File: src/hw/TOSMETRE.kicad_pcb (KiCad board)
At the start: 2 copper layers, 4.5 x 3.5 mm, 61 parts, among them J1 Barrel_Jack_Switch, J2 Conn_01x02_Male, J3 Conn_01x08_Male, J4 Conn_Coaxial, J5 Conn_01x05_Male, J6 Conn_01x02_Male, J7 Conn_Coaxial, SW1 SW_DIP_x01, U1 TPS70950DBVT, U2 18F1320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

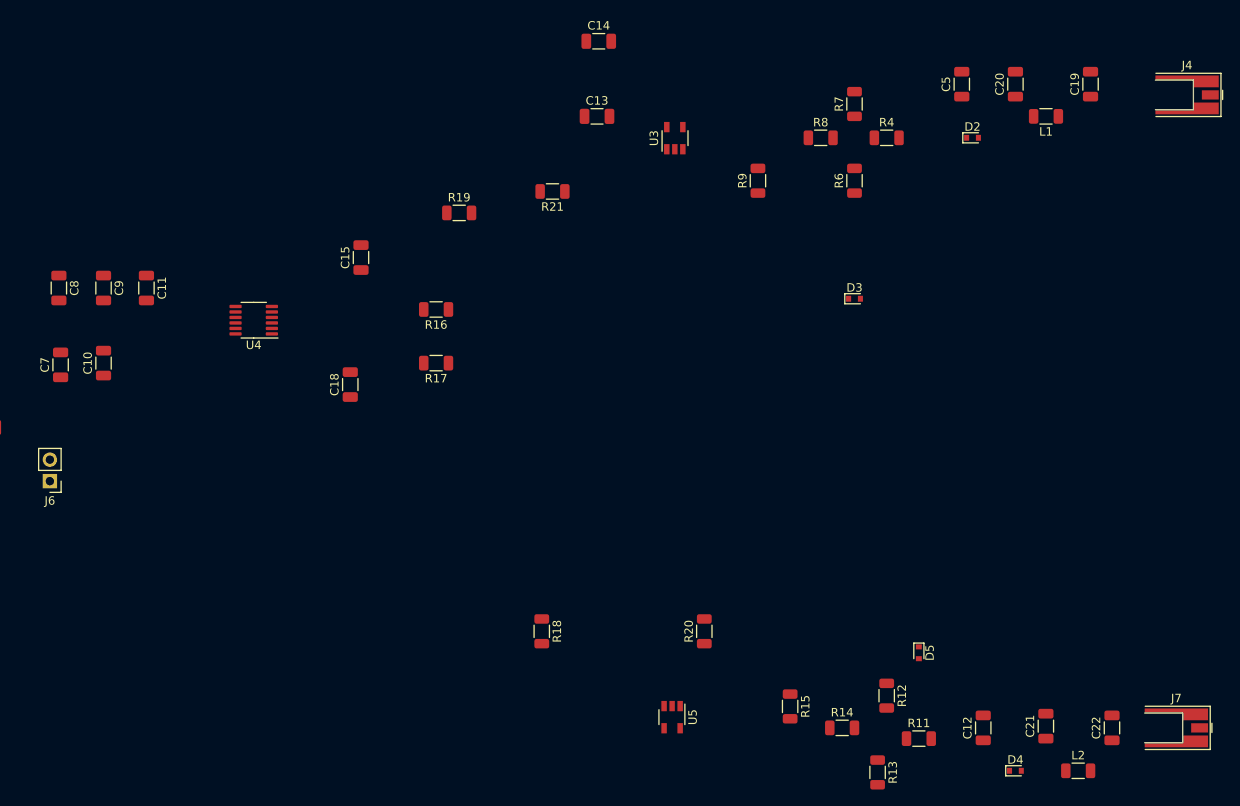
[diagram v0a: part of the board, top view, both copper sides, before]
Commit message: #305
debut routage pour degrossir et se rendre compte
a optimiser
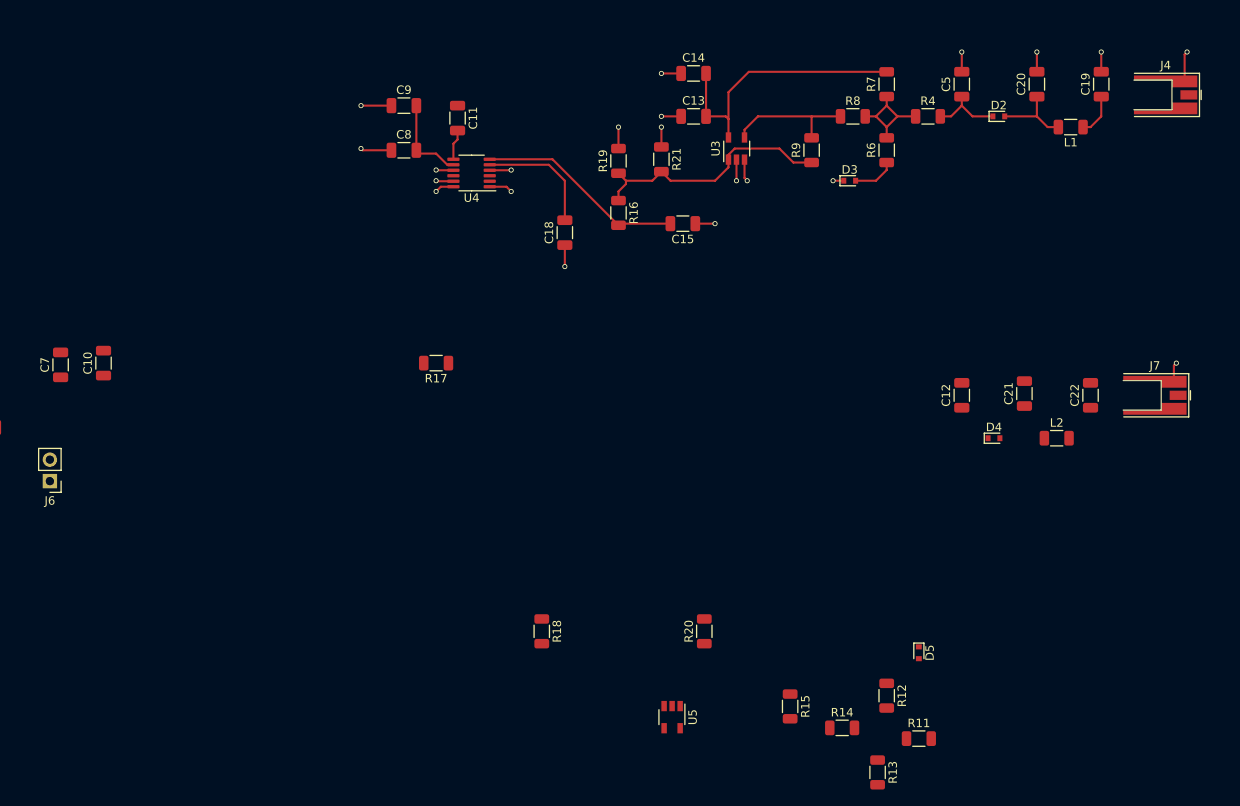
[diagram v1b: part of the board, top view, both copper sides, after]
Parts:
- moved C8 44.0 mm to (166.4, 45.9), turned to 0 degrees
- moved C11 42.0 mm to (172.7, 42.1)
- moved C9 41.6 mm to (166.4, 40.6), turned to 0 degrees
- moved C21 39.5 mm to (239.8, 74.7)
- moved C12 39.5 mm to (232.4, 74.9)
- moved C22 39.5 mm to (247.7, 74.9)
- moved D4 39.5 mm to (236.2, 80.0)
- moved J7 39.5 mm to (255.3, 74.9)
- moved L2 39.5 mm to (243.6, 80.0)
- moved C15 38.3 mm to (199.4, 54.6), turned to 180 degrees
- moved U4 31.1 mm to (174.4, 48.6)
- moved C18 31.1 mm to (185.4, 55.7)
- moved R16 24.4 mm to (191.8, 53.3), turned to 270 degrees
- moved R19 19.8 mm to (191.8, 47.2), turned to 90 degrees
- moved D3 14.0 mm to (219.1, 49.5)
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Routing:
- net GNDREF: track 0.00 -> 52.8 mm, vias 0 -> 21
- net Net-(C13-Pad2): track 0.00 -> 33.0 mm
- net Net-(R16-Pad1): track 0.00 -> 30.0 mm
- net Net-(C15-Pad2): track 0.00 -> 24.7 mm
- net Net-(R8-Pad1): track 0.00 -> 15.5 mm
- net Net-(C18-Pad2): track 0.00 -> 14.3 mm
- net Net-(R4-Pad1): track 0.00 -> 13.0 mm
- net Net-(C8-Pad2): track 0.00 -> 10.4 mm
- net Net-(C20-Pad1): track 0.00 -> 9.21 mm
- net Net-(C5-Pad1): track 0.00 -> 8.34 mm
- net Net-(D3-Pad2): track 0.00 -> 5.09 mm
- net Net-(C19-Pad1): track 0.00 -> 5.02 mm
- net Net-(C11-Pad2): track 0.00 -> 3.60 mm

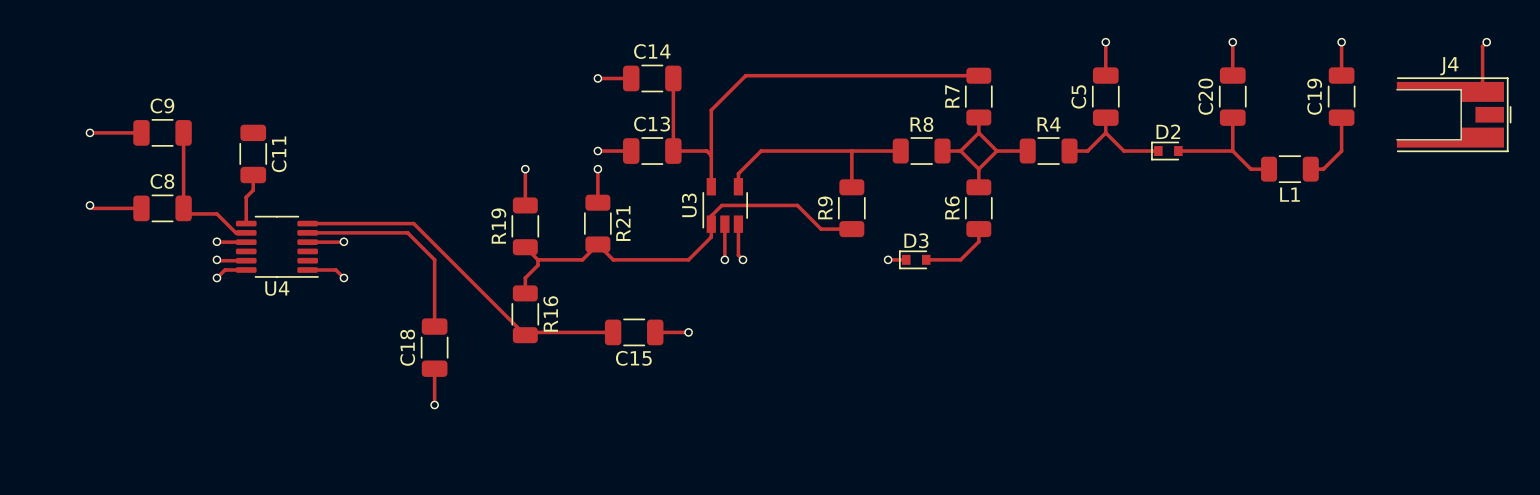
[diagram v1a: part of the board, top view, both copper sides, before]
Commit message: #305
pour validation
Pise 1mm
via  diametre 1,4 et percage de 0,6
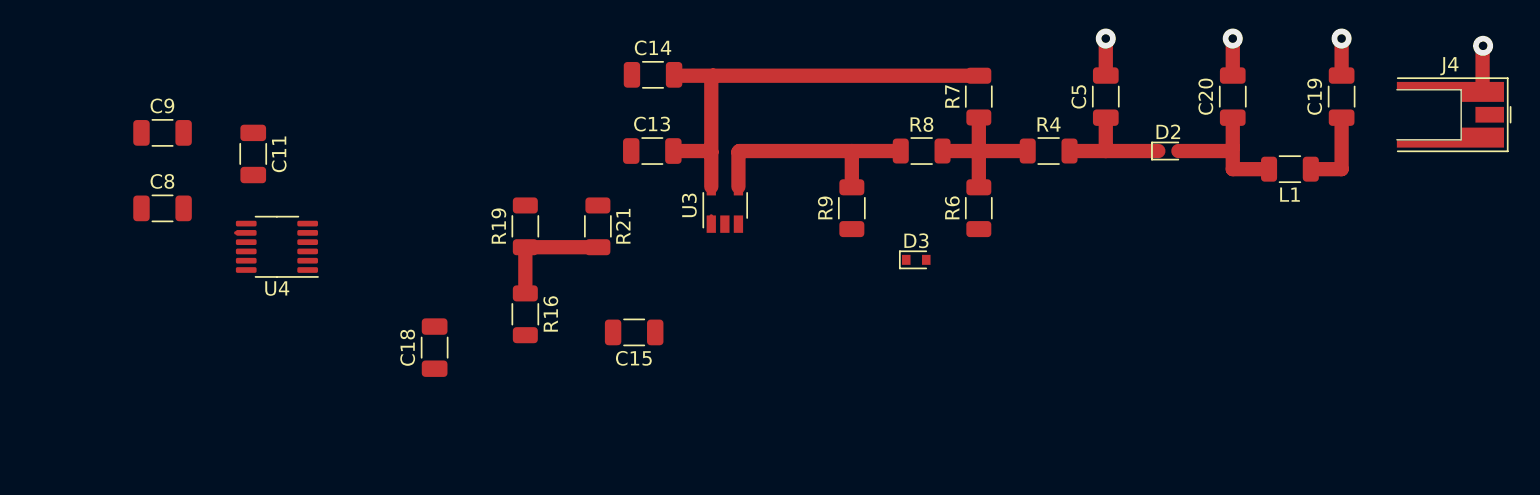
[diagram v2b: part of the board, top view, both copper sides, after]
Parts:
- moved C14 0.26 mm to (200.7, 36.6)
- moved R21 0.19 mm to (196.8, 47.2)
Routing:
- net GNDREF: track 52.8 -> 13.3 mm, vias 21 -> 5
- net Net-(C15-Pad2): track 24.7 -> 0.27 mm
- net Net-(R16-Pad1): track 30.0 -> 8.88 mm
- net Net-(C18-Pad2): track 14.3 -> 0.00 mm
- net Net-(C8-Pad2): track 10.4 -> 1.28 mm
- net Net-(D3-Pad2): track 5.09 -> 0.00 mm
- net Net-(C11-Pad2): track 3.60 -> 0.00 mm
- net Net-(R4-Pad1): track 13.0 -> 11.1 mm
- net Net-(C13-Pad2): track 33.0 -> 31.9 mm
- net Net-(R8-Pad1): track 15.5 -> 16.4 mm
- net Net-(C20-Pad1): track 9.21 -> 10.1 mm
- net Net-(C19-Pad1): track 5.02 -> 5.76 mm

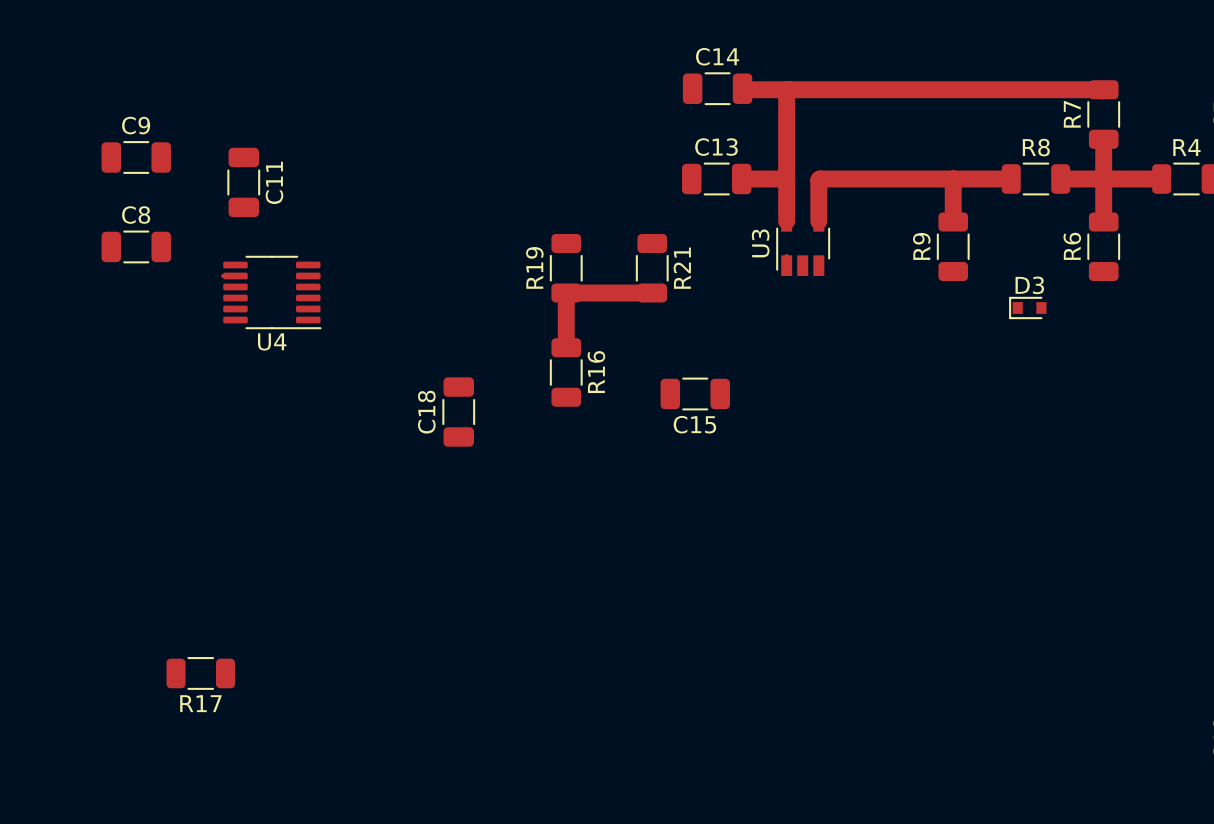
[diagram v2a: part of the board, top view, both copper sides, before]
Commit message: #305
suite du routage
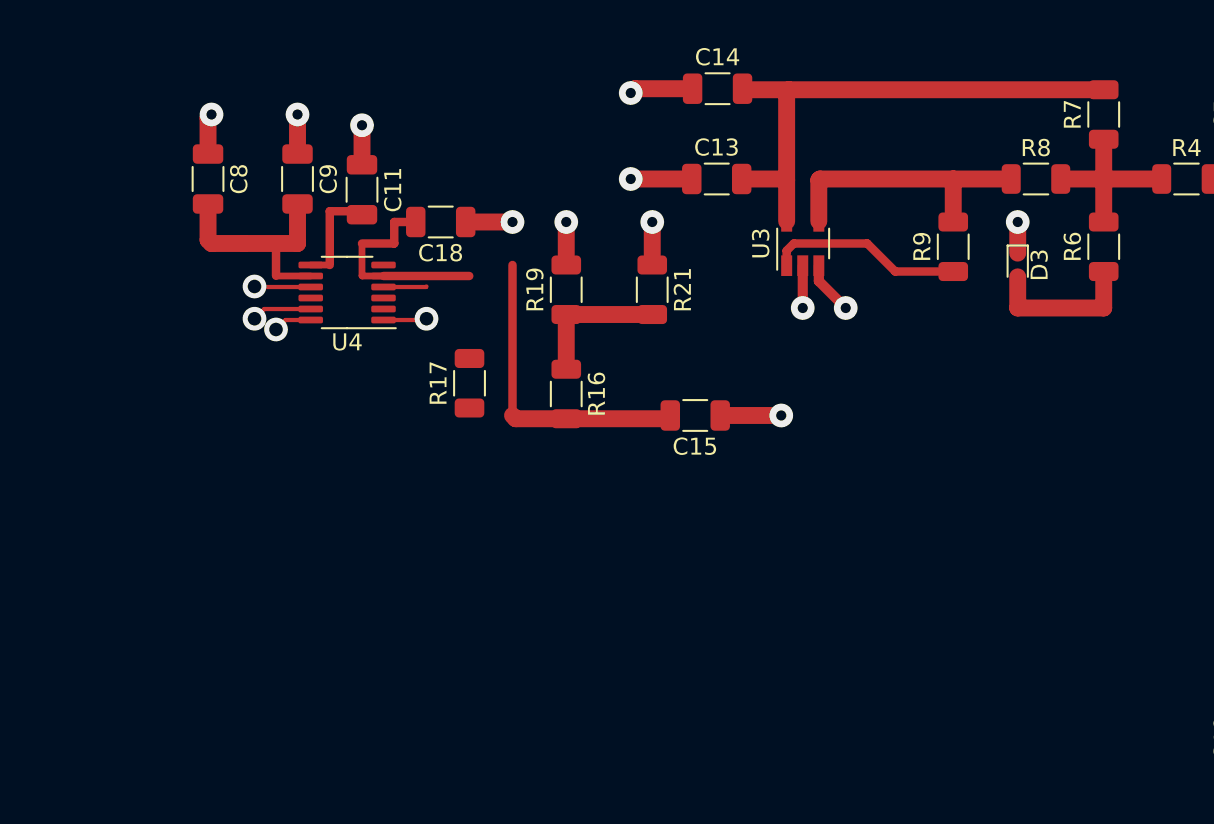
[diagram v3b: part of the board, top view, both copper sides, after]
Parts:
- moved R17 23.4 mm to (186.1, 54.0), turned to 90 degrees
- moved C18 11.3 mm to (184.4, 44.5), turned to 180 degrees
- moved C9 9.61 mm to (175.9, 41.9), turned to 270 degrees
- moved C11 7.00 mm to (179.7, 42.5)
- moved C8 5.84 mm to (170.6, 41.9), turned to 270 degrees
- moved U4 4.44 mm to (178.8, 48.6)
- moved D3 2.63 mm to (218.4, 47.0), turned to 270 degrees
- moved C15 1.27 mm to (199.4, 55.9)
- moved R19 1.27 mm to (191.8, 48.5)
- moved R21 1.27 mm to (196.8, 48.5)
- moved R16 1.27 mm to (191.8, 54.6)
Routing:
- net GNDREF: track 13.3 -> 61.0 mm, vias 5 -> 21
- net Net-(C15-Pad2): track 0.27 -> 18.6 mm
- net Net-(C8-Pad2): track 1.28 -> 14.3 mm
- net Net-(C18-Pad2): track 0.00 -> 12.7 mm
- net Net-(R16-Pad1): track 8.88 -> 20.5 mm
- net Net-(D3-Pad2): track 0.00 -> 9.08 mm
- net Net-(C11-Pad2): track 0.00 -> 6.29 mm

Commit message: #305
ROUTAGE

Apres je ne sais pas comment je peux faire
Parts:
- moved J3 129.4 mm to (149.5, 43.6), turned to 270 degrees
- moved J2 89.1 mm to (105.5, 88.6), turned to 270 degrees
- moved C16 84.5 mm to (109.3, 95.5), turned to 90 degrees
- moved J1 79.1 mm to (94.1, 88.6), turned to 270 degrees
- moved SW1 78.0 mm to (98.9, 85.2), turned to 270 degrees
- moved C17 69.1 mm to (118.1, 95.4), turned to 90 degrees
- moved D1 66.1 mm to (91.7, 95.9), turned to 270 degrees
- moved C1 58.2 mm to (96.4, 96.0), turned to 270 degrees
- moved C4 54.7 mm to (113.0, 95.4), turned to 270 degrees
- moved U1 52.7 mm to (101.9, 95.4)
- moved J5 47.6 mm to (142.0, 22.5)
- moved C7 46.9 mm to (166.1, 47.5), turned to 270 degrees
- moved U2 42.1 mm to (144.8, 71.4)
- moved C2 38.4 mm to (122.6, 95.4)
- moved C10 38.3 mm to (161.0, 47.5), turned to 270 degrees
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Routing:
- net Net-(C10-Pad2): track 0.00 -> 243.8 mm
- net GNDREF: track 61.0 -> 146.0 mm, vias 21 -> 47
- net Net-(J3-Pad7): track 0.00 -> 55.6 mm
- net Net-(R15-Pad1): track 0.00 -> 54.0 mm
- net Net-(J3-Pad6): track 0.00 -> 52.4 mm
- net Net-(C6-Pad1): track 0.00 -> 43.0 mm
- net Net-(J3-Pad2): track 0.00 -> 30.2 mm
- net Net-(R14-Pad1): track 0.00 -> 29.7 mm
- net Net-(J3-Pad5): track 0.00 -> 28.1 mm
- net Net-(J3-Pad3): track 0.00 -> 27.8 mm
- net Net-(J3-Pad4): track 0.00 -> 24.9 mm
- net (no net): track 0.00 -> 21.1 mm
- net Net-(D1-Pad2): track 0.00 -> 13.3 mm
- net Net-(J1-Pad3): track 0.00 -> 12.1 mm
- net Net-(C12-Pad1): track 0.00 -> 10.6 mm
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
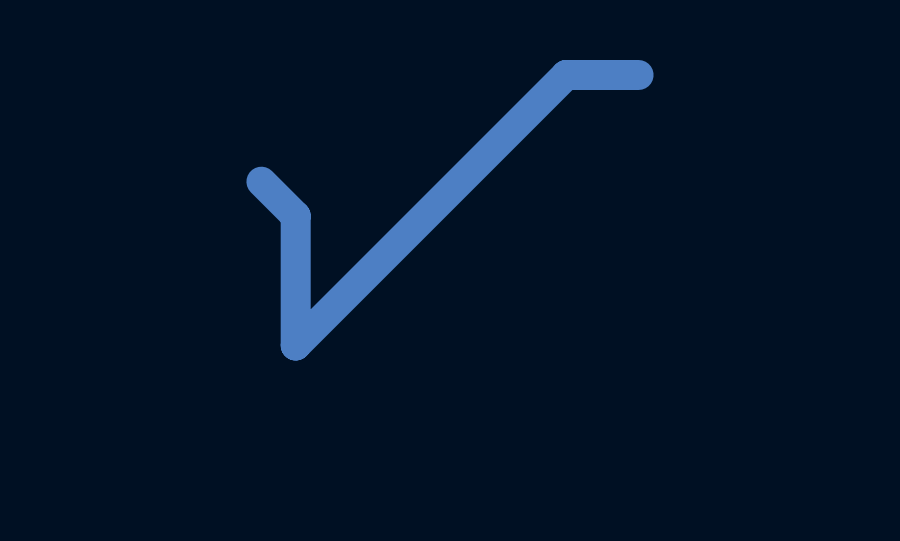
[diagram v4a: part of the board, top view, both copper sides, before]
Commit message: #305
MODIFICATION EMPREINTE J3 J5 ET J2
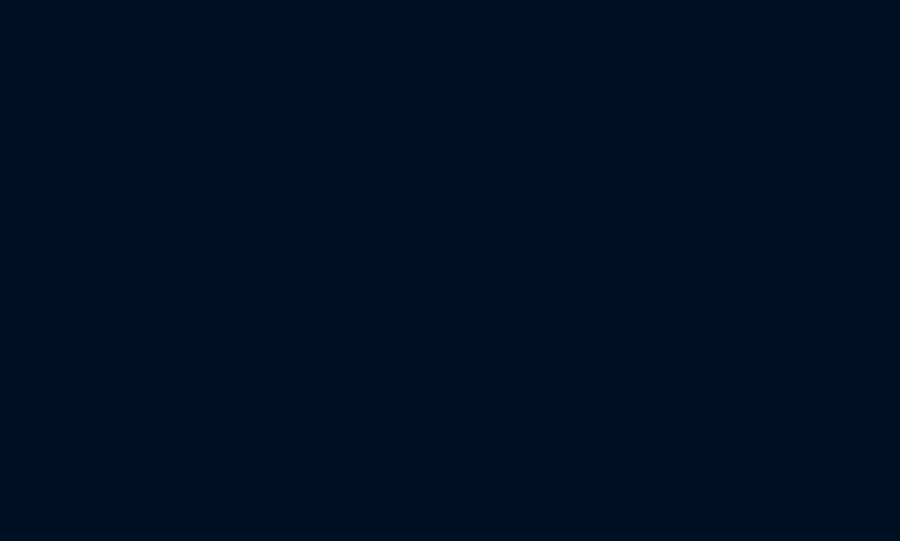
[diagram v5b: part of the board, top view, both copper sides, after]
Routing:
- net (no net): track 21.1 -> 0.00 mm
